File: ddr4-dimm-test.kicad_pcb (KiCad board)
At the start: 2 copper layers, 133.3 x 31.2 mm, 137 parts, among them IC1 DDR4-BGA78, IC2 DDR4-BGA78, IC3 DDR4-BGA78, IC4 DDR4-BGA78, IC5 DDR4-BGA78, IC6 DDR4-BGA78, IC7 DDR4-BGA78, IC8 DDR4-BGA78

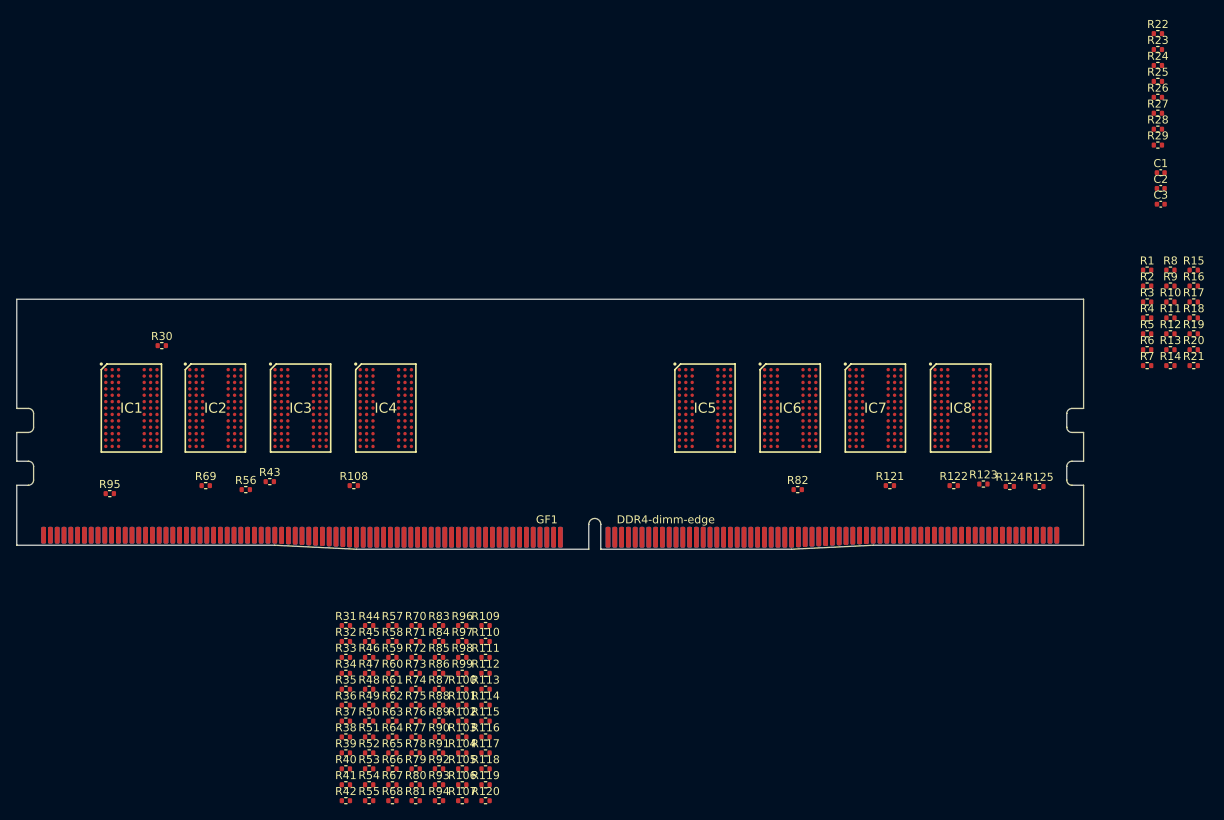
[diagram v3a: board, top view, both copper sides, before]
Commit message: some component placement
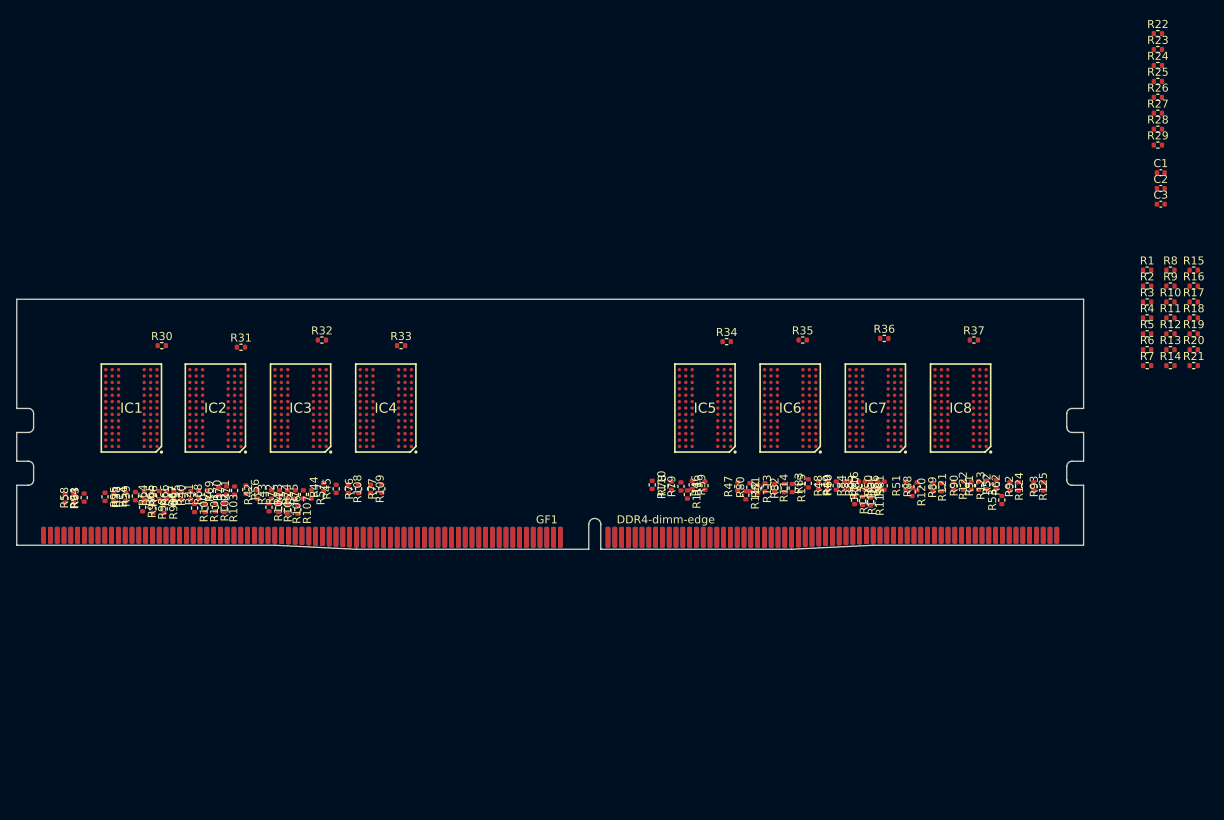
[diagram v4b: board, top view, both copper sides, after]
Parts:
- moved R37 91.8 mm to (195.0, 85.8)
- moved R53 85.9 mm to (198.5, 105.8), turned to 90 degrees
- moved R52 85.3 mm to (197.8, 103.8), turned to 90 degrees
- moved R93 84.3 mm to (203.7, 104.1), turned to 90 degrees
- moved R36 81.4 mm to (183.8, 85.6)
- moved R92 80.6 mm to (200.6, 104.1), turned to 90 degrees
- moved R62 79.2 mm to (196.6, 103.9), turned to -90 degrees
- moved R91 75.3 mm to (195.6, 104.0), turned to 90 degrees
- moved R51 74.1 mm to (186.5, 104.0), turned to 90 degrees
- moved R90 72.7 mm to (193.7, 104.0), turned to 90 degrees
- moved R35 71.9 mm to (173.6, 85.8)
- moved R50 70.1 mm to (183.0, 104.0), turned to 90 degrees
- moved R89 69.3 mm to (191.0, 104.2), turned to 90 degrees
- moved R120 65.8 mm to (187.3, 104.8), turned to -90 degrees
- moved R88 65.7 mm to (187.9, 104.1), turned to 90 degrees
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
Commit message: more component placement
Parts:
- moved R64 5.00 mm to (87.3, 105.4)
- moved R96 4.85 mm to (86.5, 105.4)
- moved R39 4.60 mm to (85.6, 105.4)
- moved R66 4.30 mm to (90.7, 105.4)
- moved R38 4.25 mm to (84.8, 105.4)
- moved R65 4.20 mm to (89.0, 105.4)
- moved R95 4.20 mm to (82.2, 105.4)
- moved R77 4.07 mm to (117.0, 105.4)
- moved R67 3.60 mm to (92.4, 105.4)
- moved R54 3.60 mm to (83.9, 105.4)
- moved R109 3.54 mm to (116.2, 105.4)
- moved R97 3.22 mm to (88.2, 105.4)
- moved R41 3.16 mm to (95.0, 105.4)
- moved R40 3.01 mm to (94.1, 105.4)
- moved R98 2.96 mm to (89.8, 105.4)
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
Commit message: Some more layout testing
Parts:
- moved R110 9.23 mm to (163.7, 106.3)
- moved R79 8.17 mm to (166.2, 106.3)
- moved R78 7.72 mm to (164.6, 106.3)
- moved R59 7.70 mm to (167.1, 106.3)
- moved R46 6.96 mm to (167.9, 106.3)
- moved R111 6.32 mm to (165.4, 106.3)
- moved IC1 5.64 mm to (85.1, 97.5)
- moved R61 4.38 mm to (185.8, 106.3)
- moved R50 4.34 mm to (186.7, 106.3)
- moved R87 4.26 mm to (184.9, 106.3)
- moved R93 4.12 mm to (200.2, 106.3)
- moved R80 4.11 mm to (170.5, 106.3)
- moved R47 3.99 mm to (168.8, 106.3)
- moved R81 3.94 mm to (172.2, 106.3)
- moved R113 3.88 mm to (171.3, 106.3)
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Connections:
- IC1 pad B7: DQ1 -> DQ4
- IC1 pad C2: DQ0 -> DQ3
- IC1 pad D2: DQ4 -> DQ7
- IC1 pad D7: DQ3 -> DQ0
- IC1 pad E7: DQ7 -> DQ1
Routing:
- net GND: track 0.00 -> 91.6 mm, vias 0 -> 25
- net DQ5: track 0.00 -> 9.23 mm
- net DQ7: track 0.00 -> 8.69 mm
- net DQ3: track 0.00 -> 8.68 mm
- net DQ1: track 0.00 -> 8.32 mm
- net DQ0: track 0.00 -> 8.25 mm
- net DQS0+: track 0.00 -> 8.07 mm, vias 0 -> 2
- net DQ2: track 0.00 -> 7.86 mm
- net DQ6: track 0.00 -> 7.74 mm
- net DQS0-: track 0.00 -> 7.66 mm, vias 0 -> 2
- net DQ4: track 0.00 -> 7.50 mm
- net VDD: track 0.00 -> 3.95 mm, vias 0 -> 1
- net Net-(GF1-DQ5): track 0.00 -> 3.33 mm, vias 0 -> 1
- net Net-(GF1-DQ0): track 0.00 -> 3.33 mm

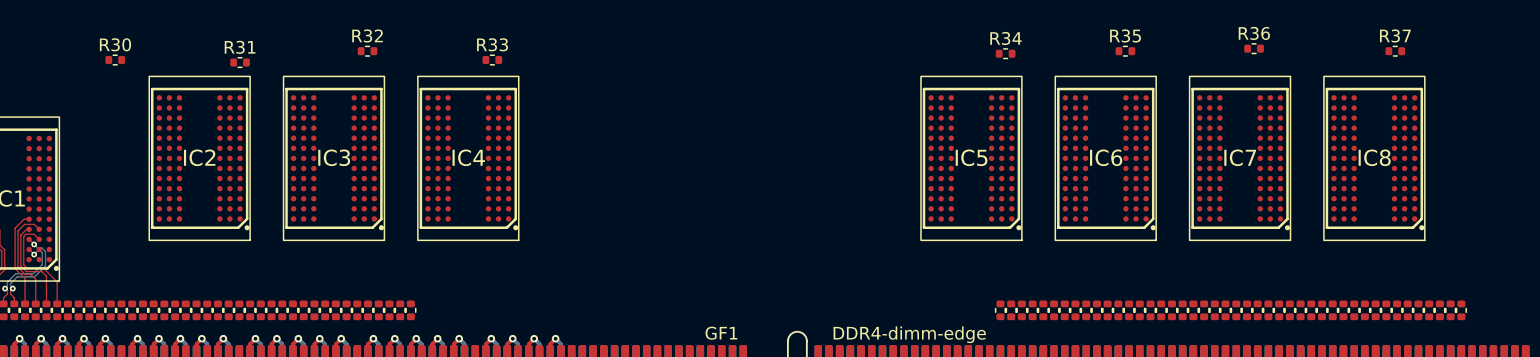
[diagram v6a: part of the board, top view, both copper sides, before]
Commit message: moved stuff and added line indicating VLP height
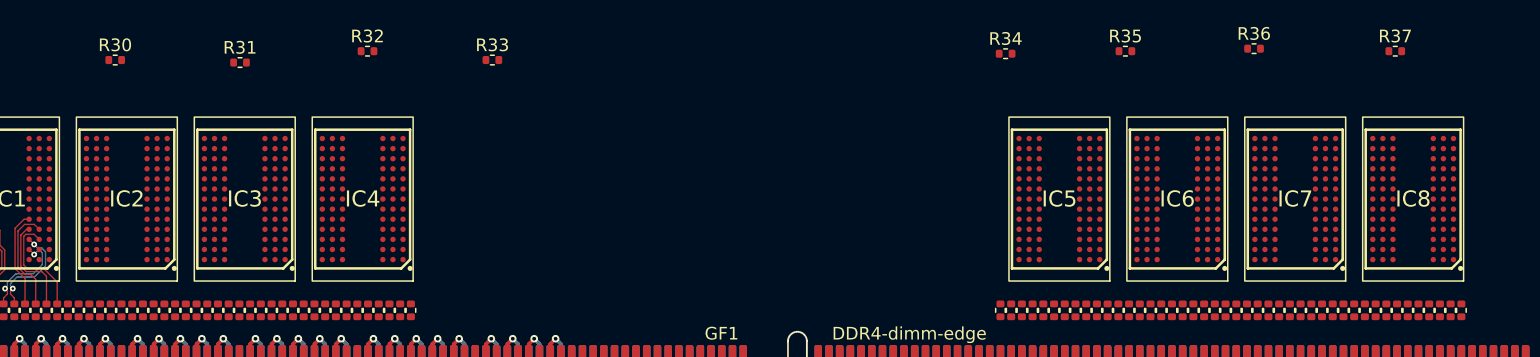
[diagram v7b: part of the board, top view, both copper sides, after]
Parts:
- moved IC4 8.97 mm to (113.1, 97.5)
- moved IC3 7.78 mm to (103.8, 97.5)
- moved IC5 7.68 mm to (168.4, 97.5)
- moved IC2 6.61 mm to (94.4, 97.5)
- moved IC6 6.53 mm to (177.7, 97.5)
- moved IC7 5.44 mm to (187.1, 97.5)
- moved IC8 4.46 mm to (196.4, 97.5)
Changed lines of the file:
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@@
 	(footprint "A_my_stuff:DDR4-BGA78"
 		(layer "F.Cu")
-		(at 100.2 94.3 180)
+		(at 94.425 97.525 180)
 		(descr "78-Ball FBGA – x4, x8 (SA)")
 		(tags "Integrated Circuit")
@@
 	(footprint "A_my_stuff:DDR4-BGA78"
 		(layer "F.Cu")
-		(at 182.7 94.3 180)
+		(at 187.075 97.525 180)
 		(descr "78-Ball FBGA – x4, x8 (SA)")
 		(tags "Integrated Circuit")
@@
 	(footprint "A_my_stuff:DDR4-BGA78"
 		(layer "F.Cu")
-		(at 172.05 94.3 180)
+		(at 177.725 97.525 180)
 		(descr "78-Ball FBGA – x4, x8 (SA)")
 		(tags "Integrated Circuit")
@@
 	(footprint "A_my_stuff:DDR4-BGA78"
 		(layer "F.Cu")
-		(at 161.4 94.3 180)
+		(at 168.375 97.525 180)
 		(descr "78-Ball FBGA – x4, x8 (SA)")
 		(tags "Integrated Circuit")
@@
 	(footprint "A_my_stuff:DDR4-BGA78"
 		(layer "F.Cu")
-		(at 110.85 94.3 180)
+		(at 103.775 97.525 180)
 		(descr "78-Ball FBGA – x4, x8 (SA)")
 		(tags "Integrated Circuit")
@@
 	(footprint "A_my_stuff:DDR4-BGA78"
 		(layer "F.Cu")
-		(at 121.5 94.3 180)
+		(at 113.125 97.525 180)
 		(descr "78-Ball FBGA – x4, x8 (SA)")
 		(tags "Integrated Circuit")
@@
 	(footprint "A_my_stuff:DDR4-BGA78"
 		(layer "F.Cu")
-		(at 193.35 94.3 180)
+		(at 196.425 97.525 180)
 		(descr "78-Ball FBGA – x4, x8 (SA)")
 		(tags "Integrated Circuit")
@@
 		)
 	)
+	(gr_line
+		(start 212.5 93.15)
+		(end 73.625 93.15)
+		(stroke
+			(width 0.1)
+			(type default)
+		)
+		(layer "User.2")
+	)
 	(segment

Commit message: wam
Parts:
- moved R32 21.7 mm to (99.1, 102.0), turned to -90 degrees
- moved R33 21.6 mm to (108.5, 102.0), turned to -90 degrees
- moved R31 20.5 mm to (89.8, 102.0), turned to -90 degrees
- moved R30 20.3 mm to (80.4, 102.0), turned to -90 degrees
- moved R37 16.6 mm to (191.8, 102.0), turned to -90 degrees
- moved R36 16.5 mm to (182.4, 102.0), turned to -90 degrees
- moved R35 16.2 mm to (173.1, 102.0), turned to -90 degrees
- moved R34 16.0 mm to (163.7, 102.0), turned to -90 degrees
- renumbered IC1 to WAM1, IC2 to WAM2, IC3 to WAM3, IC4 to WAM4, IC5 to WAM5, IC6 to WAM6, IC7 to WAM7, IC8 to WAM8
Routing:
- net Net-(WAM5-ZQ): track 0.00 -> 1.47 mm
- net Net-(WAM3-ZQ): track 0.00 -> 1.47 mm
- net Net-(WAM8-ZQ): track 0.00 -> 1.47 mm
- net Net-(WAM7-ZQ): track 0.00 -> 1.47 mm
- net Net-(WAM6-ZQ): track 0.00 -> 1.47 mm
- net Net-(WAM4-ZQ): track 0.00 -> 1.47 mm
- net Net-(WAM2-ZQ): track 0.00 -> 1.47 mm
- net Net-(WAM1-ZQ): track 0.00 -> 1.47 mm
